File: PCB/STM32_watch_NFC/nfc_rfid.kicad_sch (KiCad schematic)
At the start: 1 part, among them U3 ST25R3916-AQWT

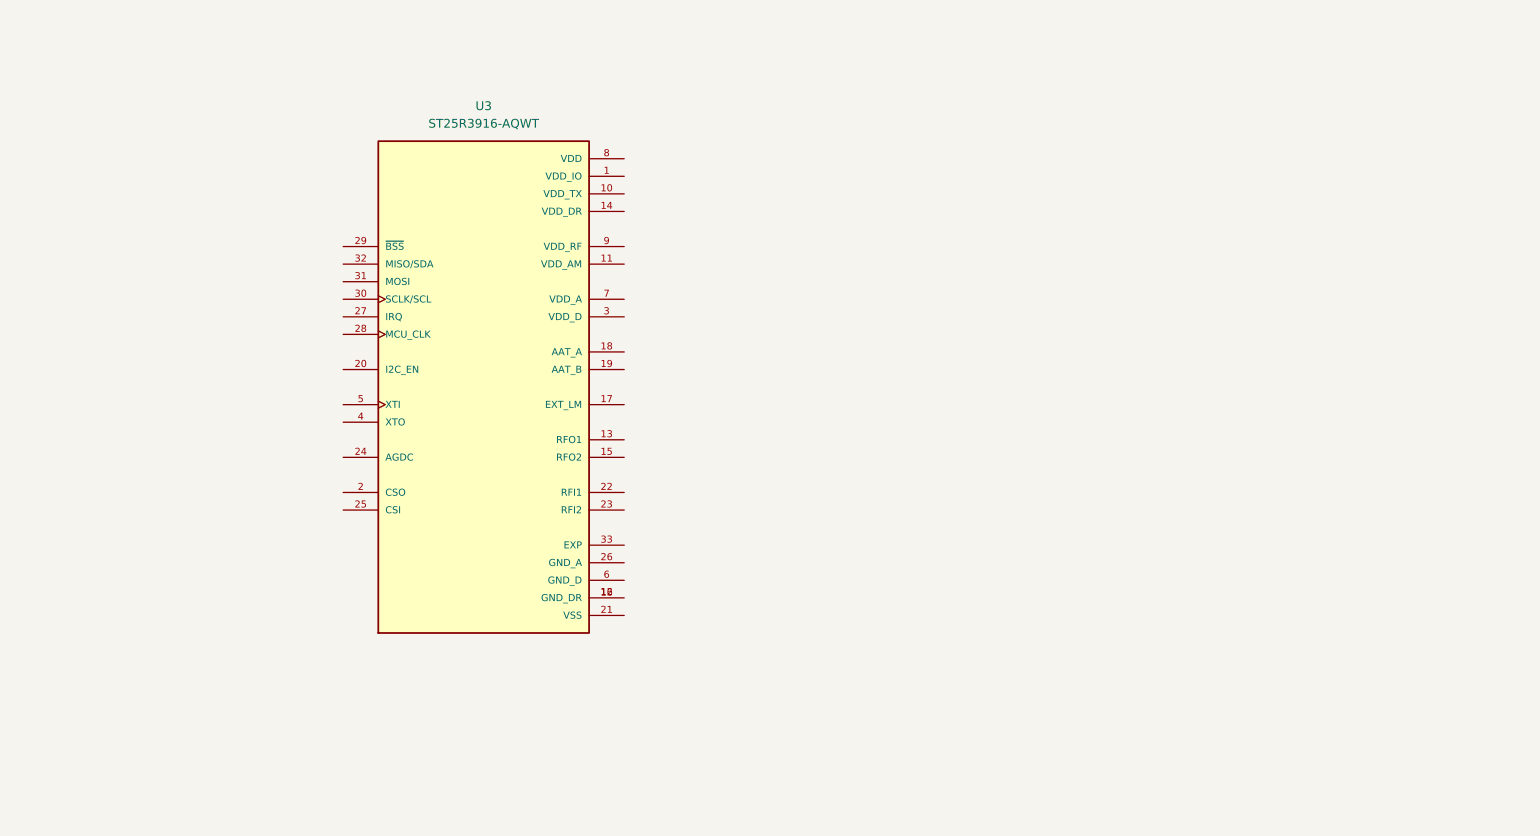
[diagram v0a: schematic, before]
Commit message: Kicad
Everything about power, started to make nfc - spiral antenna problem
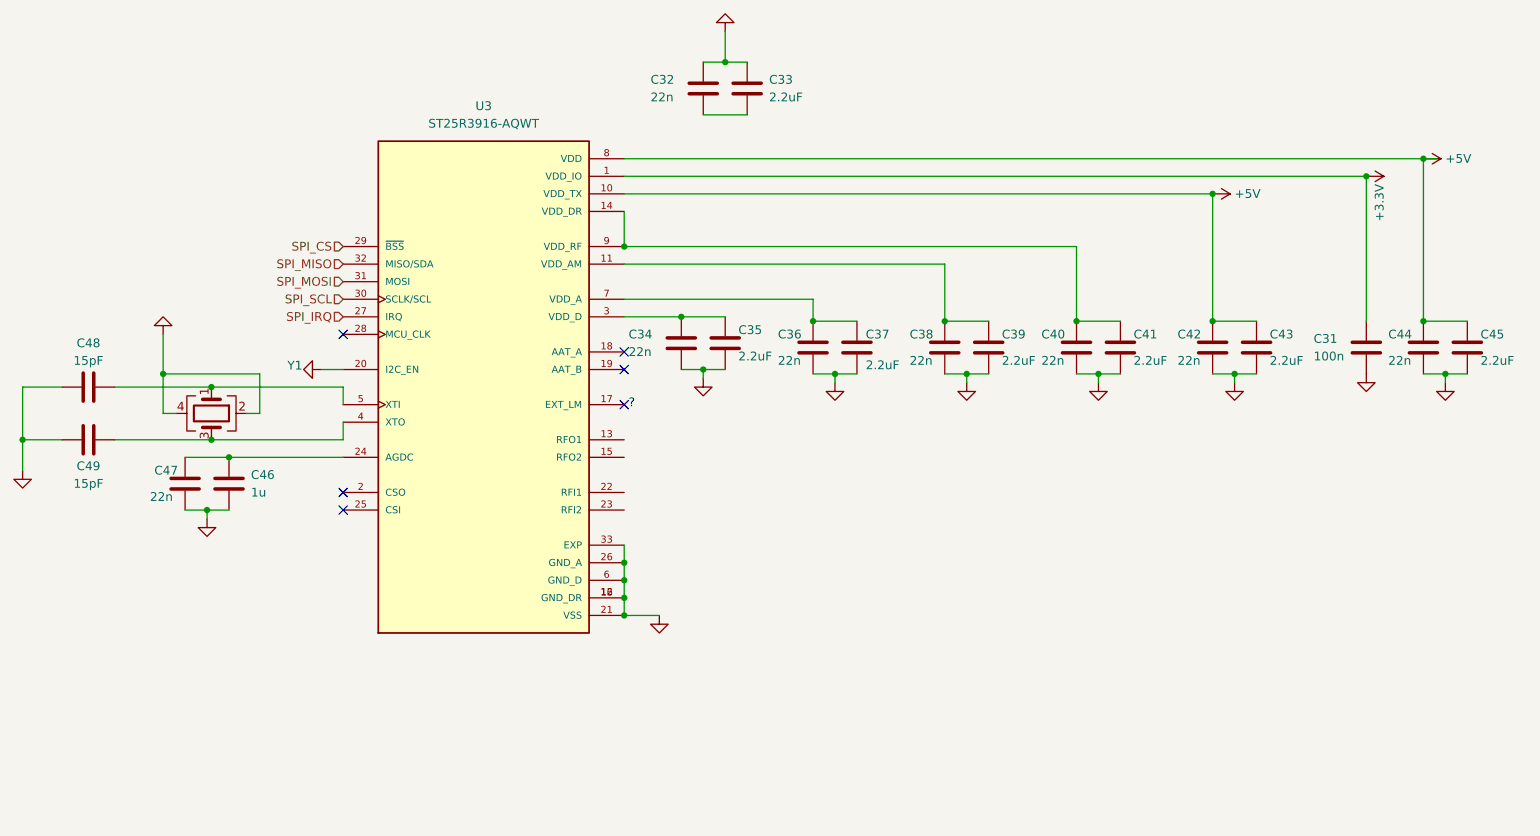
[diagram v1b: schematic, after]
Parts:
- added C31: 100n, Capacitor_SMD:C_0402_1005Metric, symbol Device:C
- added C32, C34, C36, C38, C40, C42, C44, C47: 22n, Capacitor_SMD:C_0402_1005Metric, symbol Device:C
- added C33, C35, C37, C39, C41, C43, C45: 2.2uF, Capacitor_SMD:C_0402_1005Metric, symbol Device:C
- added C46: 1u, Capacitor_SMD:C_0402_1005Metric, symbol Device:C
- added C48, C49: 15pF, Capacitor_SMD:C_0402_1005Metric, symbol Device:C
- added Y1: Crystal_GND24, symbol Device:Crystal_GND24
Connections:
- net +3.3V: now reaches U3.1 (VDD_IO)
- net +3.3V: now also C31.1
- net +5V: now reaches U3.10 (VDD_TX)
- net +5V: now also U3.8 (VDD), C42.1, C43.2, C44.1, C45.2
- net at U3.11 (VDD_AM): now also C38.1, C39.2
- net GND: now reaches U3.12 (GND_DR), U3.16 (GND_DR)
- net GND: now also U3.20 (I2C_EN), U3.21 (VSS), U3.26 (GND_A), U3.33 (EXP), U3.6 (GND_D), C31.2, C32.1, C33.2, C34.2, C35.1, C36.2, C37.1, C38.2, C39.1, C40.2, C41.1, C42.2, C43.1, C44.2, C45.1, C46.1, C47.2, C48.1, C49.1, Y1.2, Y1.4
- net at U3.14 (VDD_DR): now also U3.9 (VDD_RF), C40.1, C41.2
- net at U3.24 (AGDC): now also C46.2, C47.1
- net SPI_IRQ: now reaches U3.27 (IRQ)
- net SPI_CS: now reaches U3.29 (~{BSS})
- net at U3.3 (VDD_D): now also C34.1, C35.2
- net SPI_SCL: now reaches U3.30 (SCLK/SCL)
- net SPI_MOSI: now reaches U3.31 (MOSI)
- net SPI_MISO: now reaches U3.32 (MISO/SDA)
- net at U3.4 (XTO): now also C49.2, Y1.3
- net at U3.5 (XTI): now also C48.2, Y1.1
- net at U3.7 (VDD_A): now also C36.1, C37.2
- new net: C32.2, C33.1
- no-connect marks 0 -> 6
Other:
- note added: "?"

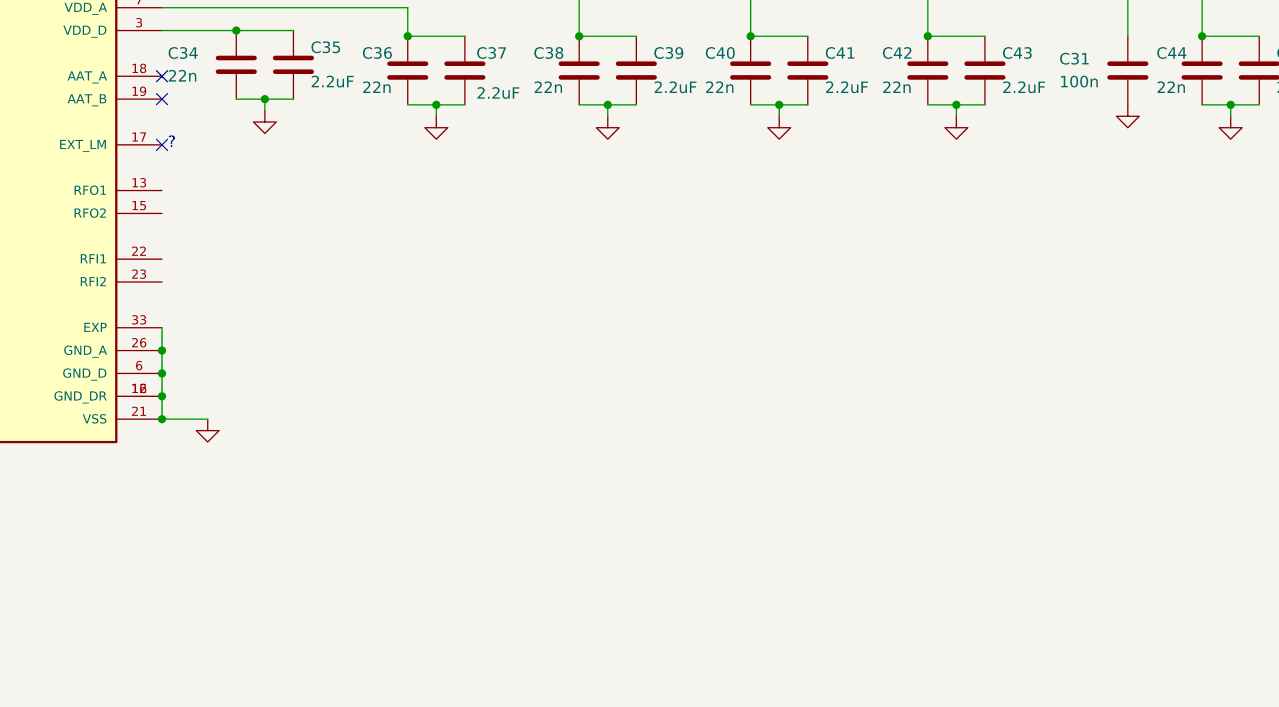
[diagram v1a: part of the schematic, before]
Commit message: NFC antenna - Kicad
I hope that antenna will work - I used TI coil designer, st25r - antenna tunning program and lots of datasheets/aplication notes
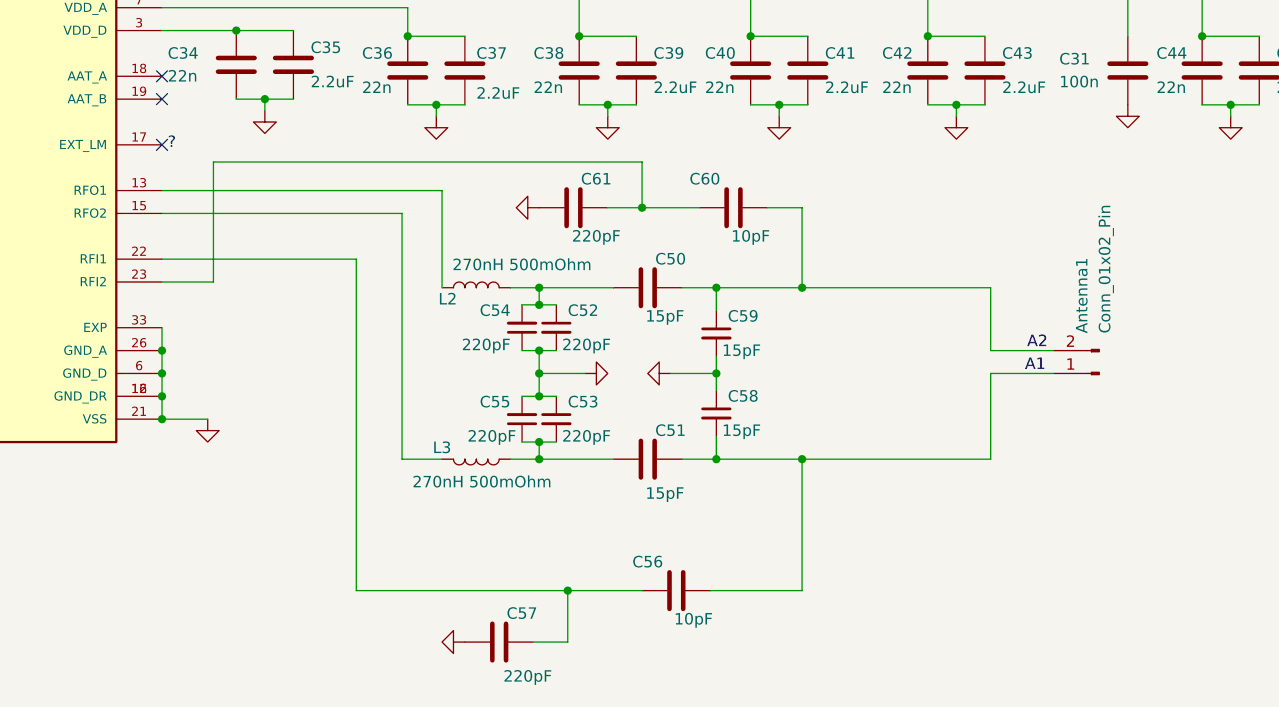
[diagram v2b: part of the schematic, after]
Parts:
- added Antenna1: Conn_01x02_Pin, symbol Connector:Conn_01x02_Pin
- added C50, C51: 15pF, Capacitor_SMD:C_0402_1005Metric, symbol Device:C
- added C52, C53, C54, C55: 220pF, Capacitor_SMD:C_0402_1005Metric, symbol Device:C_Small
- added C56, C60: 10pF, Capacitor_SMD:C_0402_1005Metric, symbol Device:C
- added C57, C61: 220pF, Capacitor_SMD:C_0402_1005Metric, symbol Device:C
- added C58, C59: 15pF, Capacitor_SMD:C_0402_1005Metric, symbol Device:C_Small
- added L2, L3: 270nH 500mOhm, symbol Device:L
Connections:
- net GND: now also C52.2, C53.1, C54.1, C55.2, C57.1, C58.1, C59.2, C61.1
- net at U3.13 (RFO1): now also L2.1
- net at U3.15 (RFO2): now also L3.2
- net at U3.22 (RFI1): now also C56.1, C57.2
- net at U3.23 (RFI2): now also C60.1, C61.2
- new net: C51.1, C53.2, C55.1, L3.1
- new net: C50.1, C52.1, C54.2, L2.2
- new net A1: Antenna1.1 (Pin_1), C51.2, C56.2, C58.2
- new net A2: Antenna1.2 (Pin_2), C50.2, C59.1, C60.2

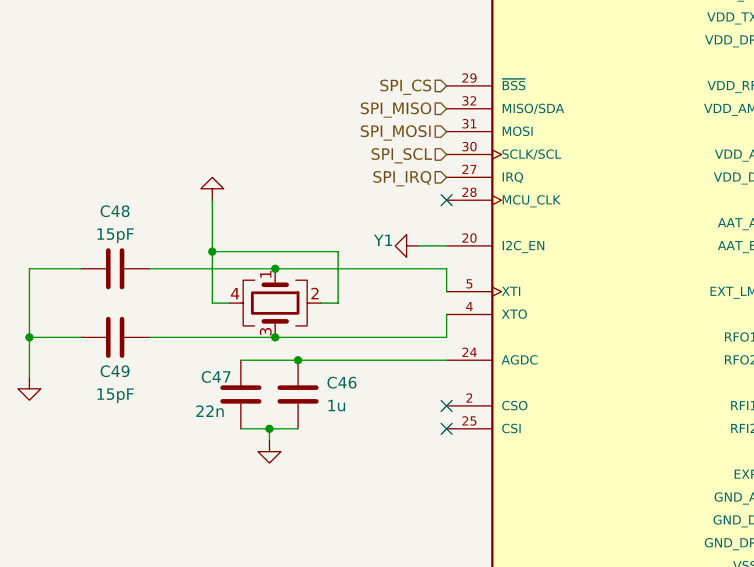
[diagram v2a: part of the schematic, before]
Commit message: Kicad - LCSC, footprints
I managed to add all (I hope so :) ) LCSC values - which component will be used. With that I could determine all footprints
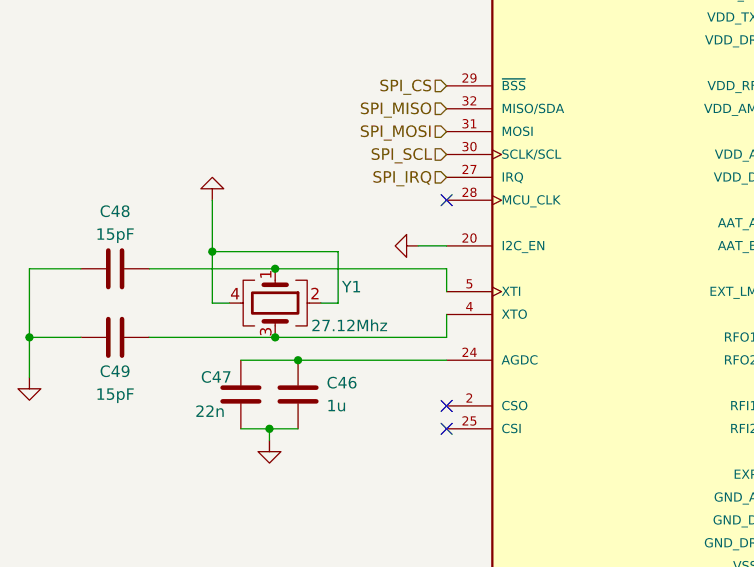
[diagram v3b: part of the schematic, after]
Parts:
- C31: footprint Capacitor_SMD:C_0402_1005Metric -> Capacitor_SMD:C_0201_0603Metric; LCSC (none) -> C7393837
- C32, C34, C36, C38, C40, C42, C44, C47: footprint Capacitor_SMD:C_0402_1005Metric -> Capacitor_SMD:C_0201_0603Metric; LCSC (none) -> C575434
- C33, C35, C37, C39, C41, C43, C45: LCSC (none) -> C710880
- C46: LCSC (none) -> C412453
- C48, C49, C50, C51, C58, C59: LCSC (none) -> C327787
- C52, C53, C54, C55, C57, C61: LCSC (none) -> C1518203
- C56, C60: LCSC (none) -> C328913
- L2, L3: footprint (none) -> Inductor_SMD:L_0805_2012Metric; LCSC (none) -> C281081
- U3: A_MAX 1.0 -> (none); Availability In Stock -> (none); B_MAX 0.3 -> (none); B_MIN 0.18 -> (none); B_NOM 0.25 -> (none); Check_prices https://www.snapeda.com/parts/ST25R3916-AQWT/STMicroelectro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 -> (none); D2_NOM 3.5 -> (none); D_MAX 5.0 -> (none); D_MIN 5.0 -> (none); D_NOM 5.0 -> (none); E2_NOM 3.5 -> (none); ENOM 0.5 -> (none); E_MAX 5.0 -> (none); E_MIN 5.0 -> (none); E_NOM 5.0 -> (none); LCSC (none) -> C5267436; L_MAX 0.5 -> (none); L_MIN 0.3 -> (none); L_NOM 0.4 -> (none); MANUFACTURER STMicroelectronics -> (none); MF STMicroelectronics -> (none); MP ST25R3916-AQWT -> (none); PARTREV 4 -> (none); PIN_COUNT_D 8.0 -> (none); PIN_COUNT_E 8.0 -> (none); Package None -> (none); Price None -> (none); STANDARD IPC 7351B -> (none); SnapEDA_Link https://www.snapeda.com/parts/ST25R3916-AQWT/STMicroelectro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 -> (none)
- Y1: value Crystal_GND24 -> 27.12Mhz; footprint (none) -> Crystal:Crystal_SMD_3225-4Pin_3.2x2.5mm; LCSC (none) -> C251623

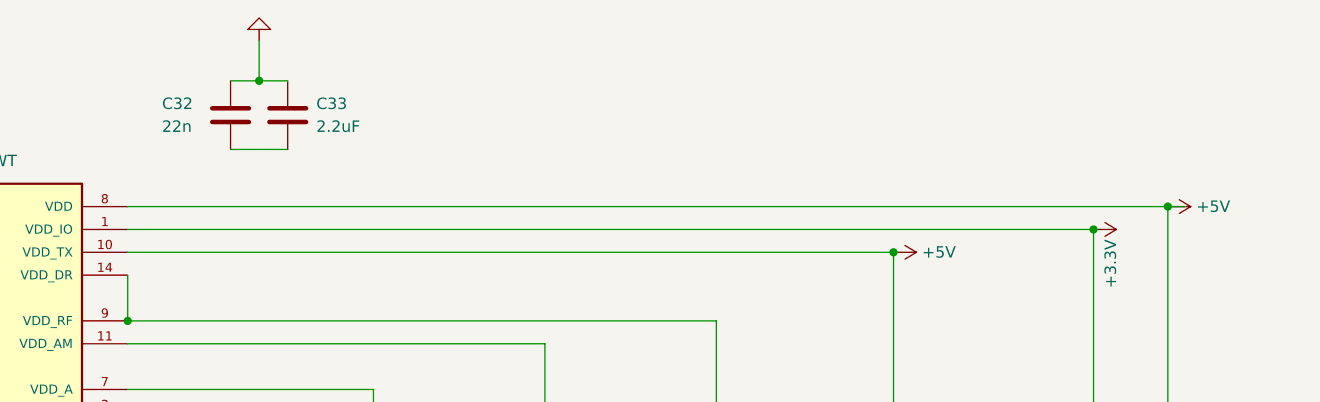
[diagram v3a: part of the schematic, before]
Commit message: Kicad - layout
I placed all components in logical way. It is NOT routed.
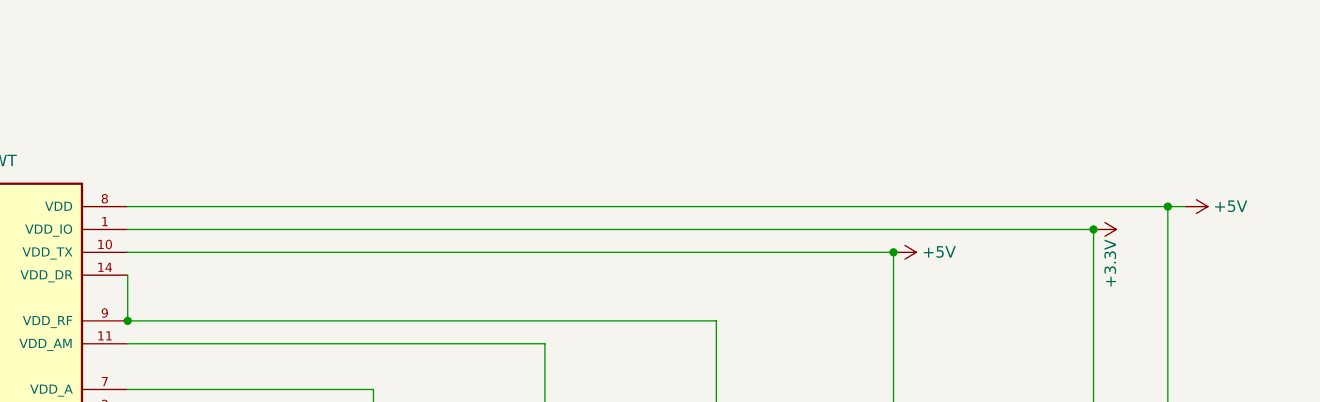
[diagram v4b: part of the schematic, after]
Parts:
- removed C32: 22n, Capacitor_SMD:C_0201_0603Metric, symbol Device:C
- removed C33: 2.2uF, Capacitor_SMD:C_0402_1005Metric, symbol Device:C
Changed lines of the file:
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@@
   (junction (at 158.115 76.835) (diameter 0) (color 0 0 0 0)
-  )
-  (junction (at 142.24 31.75) (diameter 0) (color 0 0 0 0)
   )
   (junction (at 169.545 116.205) (diameter 0) (color 0 0 0 0)
@@
     (stroke (width 0) (type default))
   )
-  (wire (pts (xy 139.065 31.75) (xy 142.24 31.75))
-    (stroke (width 0) (type default))
-  )
   (wire (pts (xy 212.725 69.215) (xy 219.075 69.215))
     (stroke (width 0) (type default))
@@
     (stroke (width 0) (type default))
   )
-  (wire (pts (xy 142.24 31.75) (xy 145.415 31.75))
-    (stroke (width 0) (type default))
-  )
   (wire (pts (xy 127.635 109.22) (xy 127.635 111.76))
     (stroke (width 0) (type default))
@@
     (stroke (width 0) (type default))
   )
-  (wire (pts (xy 142.24 31.75) (xy 142.24 27.305))
-    (stroke (width 0) (type default))
-  )
   (wire (pts (xy 196.215 76.835) (xy 199.39 76.835))
     (stroke (width 0) (type default))
@@
   )
   (wire (pts (xy 67.945 78.74) (xy 86.995 78.74))
-    (stroke (width 0) (type default))
-  )
-  (wire (pts (xy 139.065 39.37) (xy 145.415 39.37))
     (stroke (width 0) (type default))
   )
@@
     (effects (font (size 1.27 1.27)) (justify right))
   )
-  (symbol (lib_id "power:+5V") (at 243.205 45.72 270) (unit 1)
-    (in_bom yes) (on_board yes) (dnp no) (fields_autoplaced)
-    (property "Reference" "#PWR087" (at 239.395 45.72 0)
-      (effects (font (size 1.27 1.27)) hide)
-    )
-    (property "Value" "+5V" (at 246.38 45.72 90)
-      (effects (font (size 1.27 1.27)) (justify left))
-    )
-    (property "Footprint" "" (at 243.205 45.72 0)
-      (effects (font (size 1.27 1.27)) hide)
-    )
-    (property "Datasheet" "" (at 243.205 45.72 0)
+  (symbol (lib_id "power:+5V") (at 245.11 45.72 270) (unit 1)
+    (in_bom yes) (on_board yes) (dnp no) (fields_autoplaced)
+    (property "Reference" "#PWR087" (at 241.3 45.72 0)
+      (effects (font (size 1.27 1.27)) hide)
+    )
+    (property "Value" "+5V" (at 248.285 45.72 90)
+      (effects (font (size 1.27 1.27)) (justify left))
+    )
+    (property "Footprint" "" (at 245.11 45.72 0)
+      (effects (font (size 1.27 1.27)) hide)
+    )
+    (property "Datasheet" "" (at 245.11 45.72 0)
       (effects (font (size 1.27 1.27)) hide)
     )
@@
         (path "/e445874f-c7a3-43dd-b930-6bce1d4fa2ef/282b593a-b5a6-4e14-bd95-457030278cb7"
           (reference "#PWR087") (unit 1)
-        )
-      )
-    )
-  )
-  (symbol (lib_id "Device:C") (at 145.415 35.56 180) (unit 1)
-    (in_bom yes) (on_board yes) (dnp no) (fields_autoplaced)
-    (property "Reference" "C33" (at 148.59 34.29 0)
-      (effects (font (size 1.27 1.27)) (justify right))
-    )
-    (property "Value" "2.2uF" (at 148.59 36.83 0)
-      (effects (font (size 1.27 1.27)) (justify right))
-    )
-    (property "Footprint" "Capacitor_SMD:C_0402_1005Metric" (at 144.4498 31.75 0)
-      (effects (font (size 1.27 1.27)) hide)
-    )
-    (property "Datasheet" "~" (at 145.415 35.56 0)
-      (effects (font (size 1.27 1.27)) hide)
-    )
-    (property "LCSC" "C710880" (at 145.415 35.56 0)
-      (effects (font (size 1.27 1.27)) hide)
-    )
-    (pin "2")
-    (pin "1")
-    (instances
-      (project "STM32_watch_NFC"
-        (path "/e445874f-c7a3-43dd-b930-6bce1d4fa2ef/282b593a-b5a6-4e14-bd95-457030278cb7"
-          (reference "C33") (unit 1)
         )
       )
@@
     )
   )
-  (symbol (lib_id "power:GND") (at 142.24 27.305 180) (unit 1)
-    (in_bom yes) (on_board yes) (dnp no) (fields_autoplaced)
-    (property "Reference" "#PWR080" (at 142.24 20.955 0)
-      (effects (font (size 1.27 1.27)) hide)
-    )
-    (property "Value" "GND" (at 142.24 22.225 0)
-      (effects (font (size 1.27 1.27)) hide)
-    )
-    (property "Footprint" "" (at 142.24 27.305 0)
-      (effects (font (size 1.27 1.27)) hide)
-    )
-    (property "Datasheet" "" (at 142.24 27.305 0)
-      (effects (font (size 1.27 1.27)) hide)
-    )
-    (pin "1")
-    (instances
-      (project "STM32_watch_NFC"
-        (path "/e445874f-c7a3-43dd-b930-6bce1d4fa2ef/282b593a-b5a6-4e14-bd95-457030278cb7"
-          (reference "#PWR080") (unit 1)
-        )
-      )
-    )
-  )
   (symbol (lib_id "power:GND") (at 215.9 78.105 0) (unit 1)
     (in_bom yes) (on_board yes) (dnp no) (fields_autoplaced)
@@
         )
       )
-    )
-  )
-  (symbol (lib_id "Device:C") (at 139.065 35.56 0) (unit 1)
-    (in_bom yes) (on_board yes) (dnp no)
-    (property "Reference" "C32" (at 131.445 34.29 0)
-      (effects (font (size 1.27 1.27)) (justify left))
-    )
-    (property "Value" "22n" (at 131.445 36.83 0)
-      (effects (font (size 1.27 1.27)) (justify left))
-    )
-    (property "Footprint" "Capacitor_SMD:C_0201_0603Metric" (at 140.0302 39.37 0)
-      (effects (font (size 1.27 1.27)) hide)
-    )
-    (property "Datasheet" "~" (at 139.065 35.56 0)
-      (effects (font (size 1.27 1.27)) hide)
-    )
-    (property "LCSC" "C575434" (at 139.065 35.56 0)
-      (effects (font (size 1.27 1.27)) hide)
-    )
-    (pin "2")
-    (pin "1")
-    (instances
-      (project "STM32_watch_NFC"
-        (path "/e445874f-c7a3-43dd-b930-6bce1d4fa2ef/282b593a-b5a6-4e14-bd95-457030278cb7"
-          (reference "C32") (unit 1)
-        )
-      )
